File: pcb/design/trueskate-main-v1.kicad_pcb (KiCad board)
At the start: 2 copper layers, 160 x 120 mm, 62 parts, among them J1 Teensy 4.1 FEMALE 1x24, J11 Mini v1.0 / 15-hole socket, J12 Mini v1.0 / 15-hole socket, J13 Mini v1.0 / 15-hole socket, J14 Mini v1.0 / 15-hole socket, J15 Mini v1.0 / 15-hole socket, J16 Mini v1.0 / 15-hole socket, J2 Teensy 4.1 FEMALE 1x24, J21 MOTOR PHASES male 1x3, J22 MOTOR PHASES male 1x3, J23 MOTOR PHASES male 1x3, J24 MOTOR PHASES male 1x3, J25 MOTOR PHASES male 1x3, J26 MOTOR PHASES male 1x3, J31 SM06B-SRSS-TB, J32 SM06B-SRSS-TB, J33 SM06B-SRSS-TB, J34 SM06B-SRSS-TB, J35 SM06B-SRSS-TB, J36 SM06B-SRSS-TB, J5 12V INPUT + / -, J6 NC KILL SWITCH, U1 SN74LV125AN, U2 SN74LV125AN

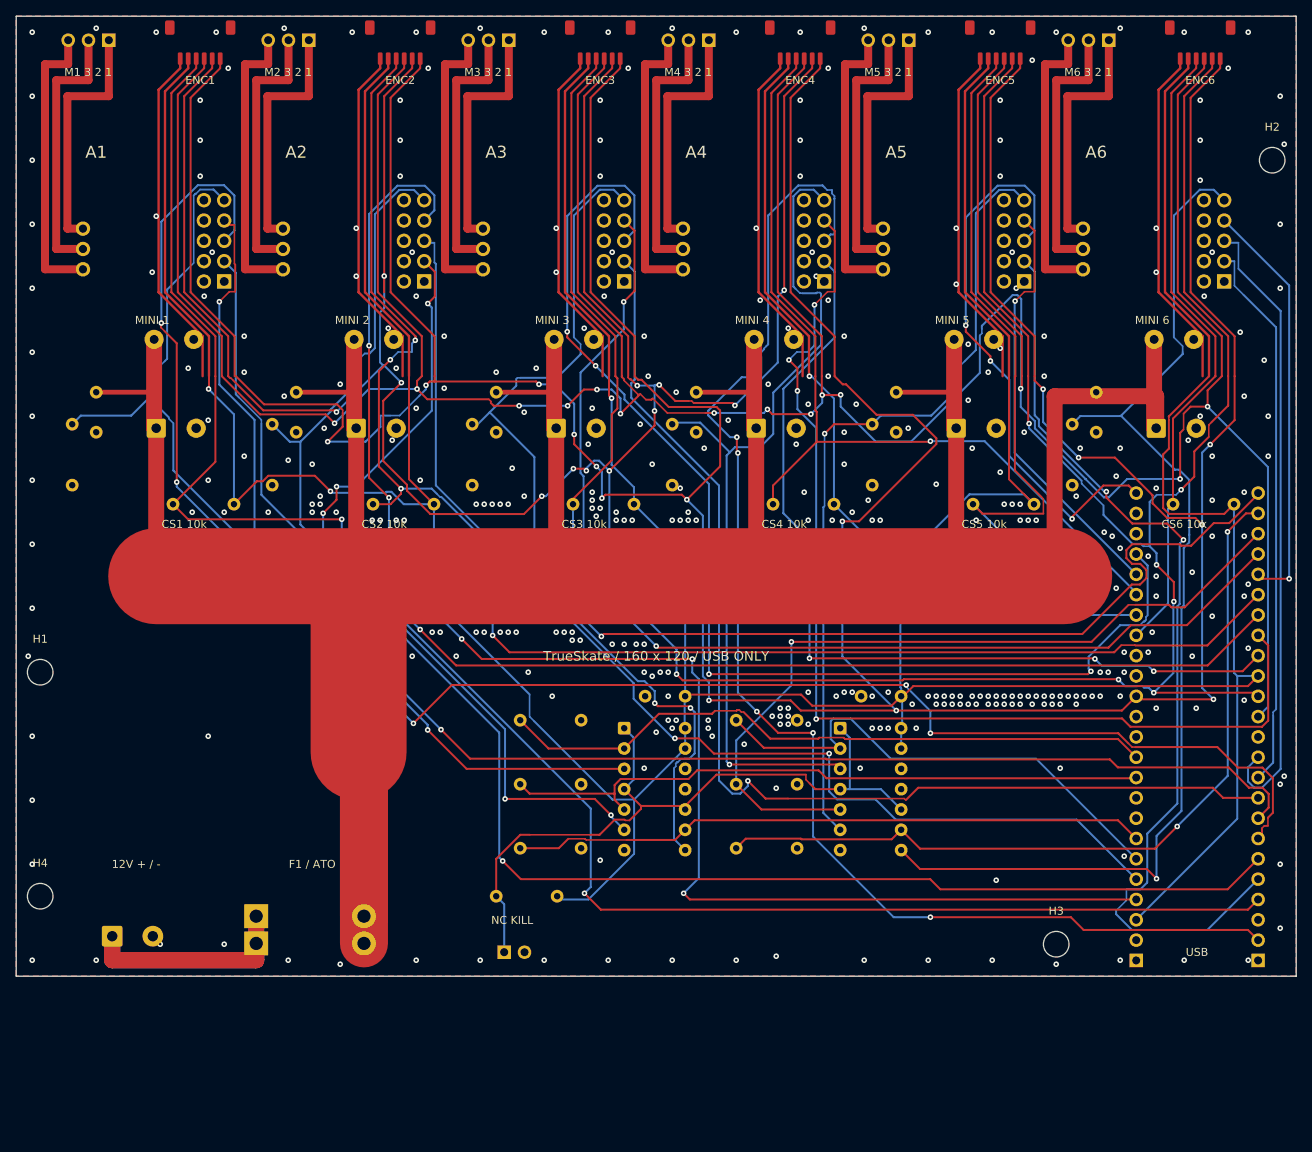
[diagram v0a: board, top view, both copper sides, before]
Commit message: feat: finalize 3+3 carrier and bare PCB fabrication package
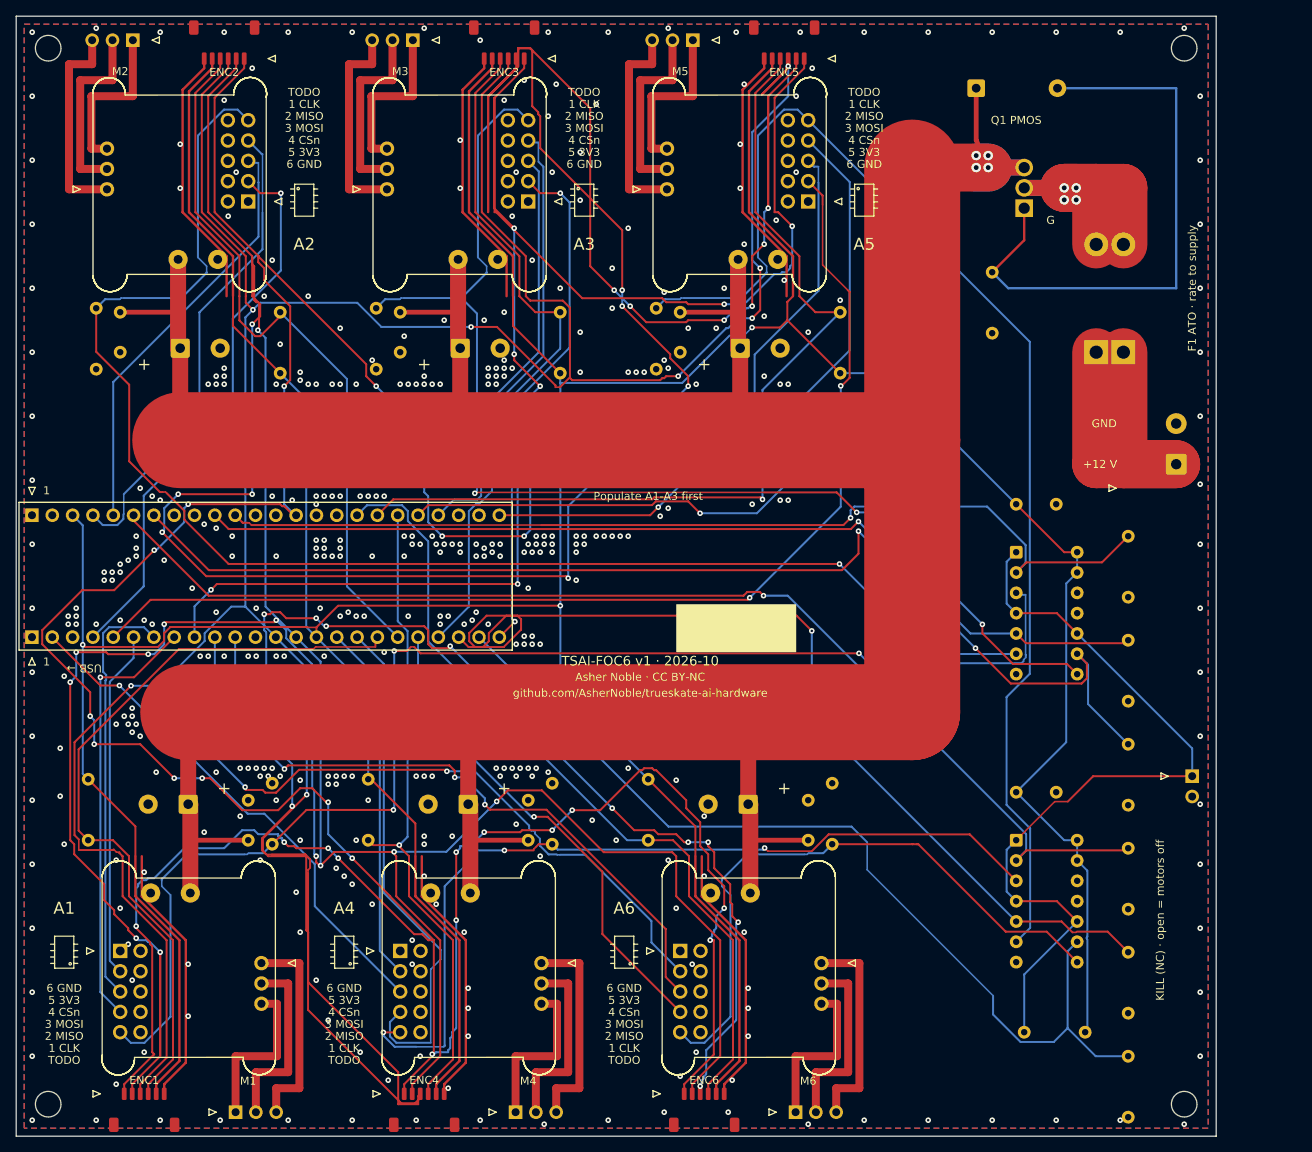
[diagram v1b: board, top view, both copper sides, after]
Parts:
- added D1: 1N4742A 12V, TrueSkate:Edge_D_DO-41_SOD81_P10.16mm_Horizontal, F.Cu at (120.0, 9.00)
- added Q1: IRF4905PBF, TrueSkate:Edge_TO-220-3_Vertical, F.Cu at (126.0, 24.0)
- added R2: 10k gate pull-down, TrueSkate:Edge_R_Axial_DIN0207_L6.3mm_D2.5mm_P7.62mm_Horizontal, F.Cu at (122.0, 32.0)
- moved J1 158.5 mm to (1.97, 77.6), turned to 90 degrees
- moved J2 148.8 mm to (1.97, 62.4), turned to 90 degrees
- moved J36 147.1 mm to (86.0, 136.7), turned to 0 degrees
- moved J5 145.5 mm to (145.0, 56.0), turned to 90 degrees
- moved J34 141.4 mm to (51.0, 136.7), turned to 0 degrees
- moved J26 139.6 mm to (97.4, 137.0), turned to 90 degrees
- moved J24 136.2 mm to (62.4, 137.0), turned to 90 degrees
- moved J21 134.9 mm to (27.4, 137.0), turned to 90 degrees
- moved J31 133.6 mm to (16.0, 136.7), turned to 0 degrees
- moved F1 126.5 mm to (135.0, 42.0), turned to 90 degrees
- moved J16 124.3 mm to (83.0, 127.0), turned to 90 degrees
- moved J14 116.7 mm to (48.0, 127.0), turned to 90 degrees
- moved J11 104.8 mm to (13.0, 127.0), turned to 90 degrees
- moved J6 88.8 mm to (147.0, 95.0), turned to 0 degrees
- moved R41 79.4 mm to (139.0, 65.0), turned to -90 degrees
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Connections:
- F1 pad 2: 12V_FUSED -> 12V_PREPOL
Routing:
- net A1_PWM2: track 218.1 -> 52.9 mm, vias 5 -> 0
- net SPI_MISO: track 545.3 -> 698.5 mm, vias 19 -> 26
- net A1_PWM1: track 186.9 -> 43.5 mm, vias 1 -> 0
- net A1_PWM3: track 187.7 -> 54.2 mm, vias 2 -> 1
- net A2_PWM3: track 188.9 -> 59.9 mm, vias 5 -> 0
- net A2_PWM1: track 186.9 -> 69.9 mm, vias 4 -> 1
- net A1_CS: track 210.4 -> 94.8 mm, vias 2 -> 0
- net A4_PWM2: track 168.5 -> 64.9 mm, vias 5 -> 1
- net A2_CS: track 191.6 -> 90.4 mm, vias 4 -> 0
- net A3_PWM2: track 149.1 -> 51.8 mm, vias 4 -> 0
- net A3_CS: track 175.6 -> 83.3 mm
- net A2_PWM2: track 143.6 -> 53.0 mm, vias 2 -> 0
- net SPI_MOSI: track 494.3 -> 583.0 mm, vias 14 -> 18
- net A4_EN_CMD: track 64.0 -> 147.3 mm, vias 0 -> 1
- net 3V3: track 701.7 -> 619.0 mm, vias 4 -> 3
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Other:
- board size 160 x 120 mm -> 150 x 140 mm
- board text added: "+"
- board text added: "+12 V"
- board text added: "1"
- board text added: "1 CLK"
- board text added: "2 MISO"
- board text added: "3 MOSI"
- board text added: "4 CSn"
- board text added: "5 3V3"
- board text added: "6 GND"
- board text added: "Asher Noble · CC BY-NC"
- board text added: "F1 ATO · rate to supply"
- board text added: "G"
- board text added: "GND"
- board text added: "KILL (NC) · open = motors off"
- board text added: "M1"
- board text added: "M2"
- board text added: "M3"
- board text added: "M4"
- board text added: "M5"
- board text added: "M6"
- board text added: "Populate A1-A3 first"
- board text added: "Q1 PMOS"
- board text added: "SD CARD SERVICE / KEEP CLEAR"
- board text added: "TODO"
- board text added: "TSAI-FOC6 v1 · 2026-10"
- board text added: "USB →"
- board text added: "github.com/AsherNoble/trueskate-ai-hardware"
- board text removed: "12V + / -"
- board text removed: "50 mm between ticks - check print scale"
- board text removed: "CS1 10k"
- board text removed: "CS2 10k"
- board text removed: "CS3 10k"
- board text removed: "CS4 10k"
- board text removed: "CS5 10k"
- board text removed: "CS6 10k"
- board text removed: "F1 / ATO"
- board text removed: "M1 3 2 1"
- board text removed: "M2 3 2 1"
- board text removed: "M3 3 2 1"
- board text removed: "M4 3 2 1"
- board text removed: "M5 3 2 1"
- board text removed: "M6 3 2 1"
- board text removed: "MINI 1"
- board text removed: "MINI 2"
- board text removed: "MINI 3"
- board text removed: "MINI 4"
- board text removed: "MINI 5"
- board text removed: "MINI 6"
- board text removed: "NC KILL"
- board text removed: "TOP VIEW / PRINT 100% / NOT MIRRORED"
- board text removed: "TrueSkate / 160 x 120 / USB ONLY"
- board text removed: "USB"

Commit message: chore: update buffer selection, sourcing BOM and repository rules
Select TI SN74HC125N C2890 without layout changes and document the unresolved powered-off EN guarantee.

- Update design metadata, BOMs, assembly planning and EN verification.

- Include the formatted sourcing workbook and purchasing documentation.

- Add the requested commit and push rules.
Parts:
- U1, U2: value SN74LV125AN -> SN74HC125N
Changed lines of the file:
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@@
 			)
 		)
-		(property "Value" "SN74LV125AN"
+		(property "Value" "SN74HC125N"
 			(at 3.81 17.57 0)
 			(layer "F.Fab")
@@
 			)
 		)
-		(property "Value" "SN74LV125AN"
+		(property "Value" "SN74HC125N"
 			(at 3.81 17.57 0)
 			(layer "F.Fab")
